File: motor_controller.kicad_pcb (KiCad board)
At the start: 2 copper layers, 251.5 x 106.7 mm, 134 parts, among them J1 STM32F4_Discovery_Header, J10 Conn_01x02_Male, J11 Conn_01x02_Male, J12 Conn_01x03_Male, J13 Conn_01x06_Male, J14 Conn_01x02_Male, J15 Conn_01x02_Male, J16 pololu-D24V10F5, J17 Conn_01x02_Male, J2 Conn_01x02_Male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

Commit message: Add memes. Also fix silkscreen
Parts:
- added G***: LOGO, roboarm_kicadlib:spanish, F.Cu at (73.7, 116.2)
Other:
- board text added: "Jos tää kaataa skumppaa stimussa niin sit mä oon vittu nähnyt kaiken. Kahdesti. -Eipou"
- board text added: "Roboarm Motor Controller Revision A Eipou 2018"

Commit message: Add controller din mount part and 3D model
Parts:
- removed G***: LOGO, roboarm_kicadlib:spanish
- removed MH3, MH4: MountingHole, MountingHole:MountingHole_3.2mm_M3_DIN965
- MH1, MH2: value MountingHole -> DinMount; footprint MountingHole:MountingHole_3.2mm_M3_DIN965 -> roboarm_kicadlib:controller_din_mount
- moved MH1 48.2 mm to (20.3, 106.7)
- moved MH2 48.2 mm to (261.6, 106.7)

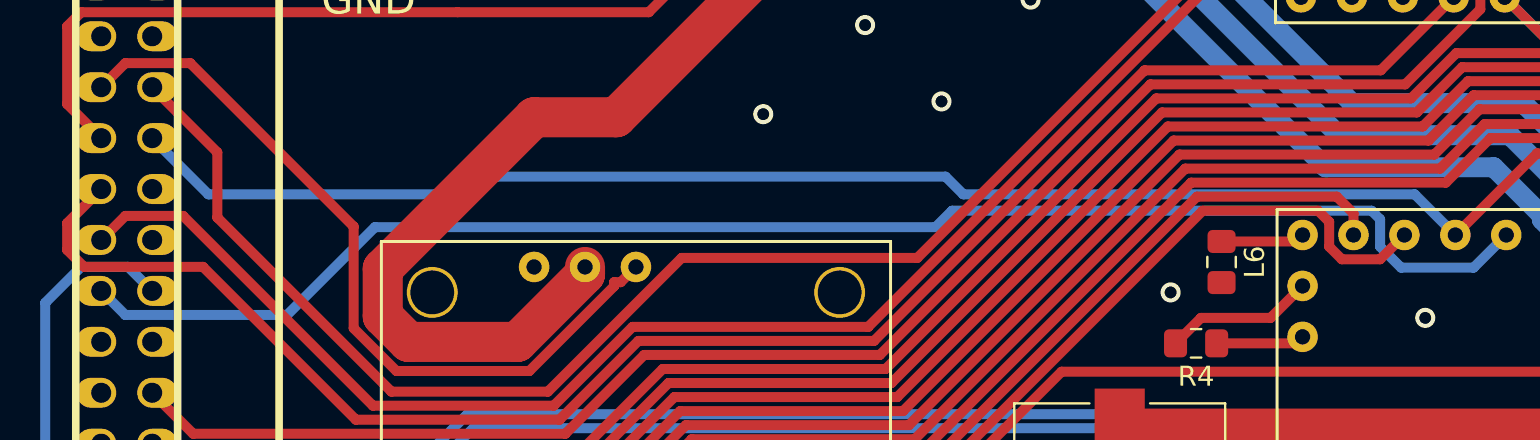
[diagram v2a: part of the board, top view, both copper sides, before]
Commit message: Add pulldown to ~motor_sleep_all
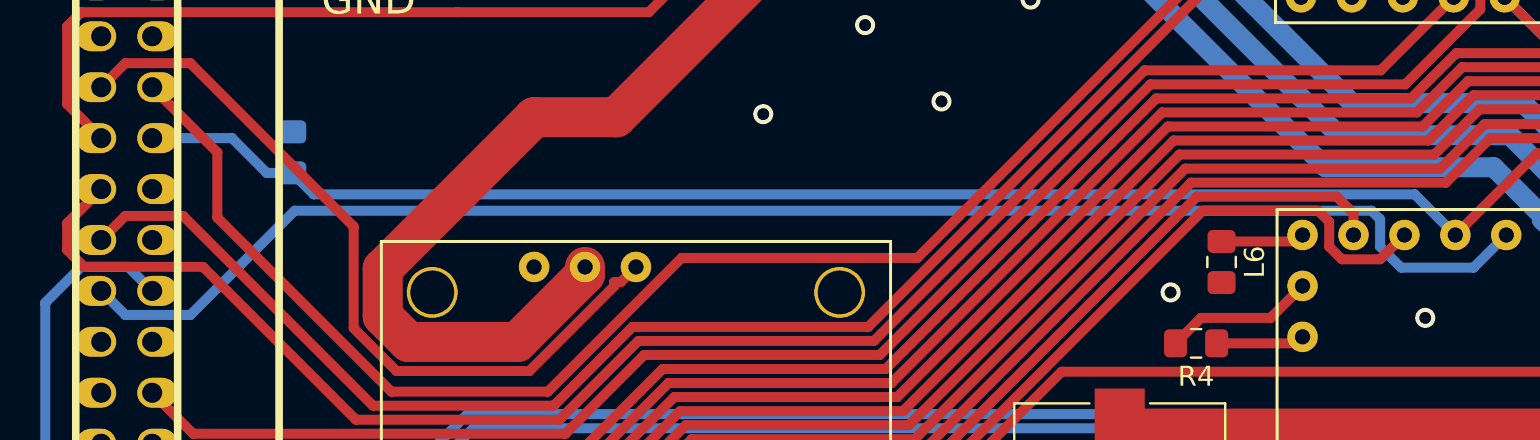
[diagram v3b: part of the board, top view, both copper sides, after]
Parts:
- added R13: 330R, Resistor_SMD:R_0805_2012Metric_Pad1.15x1.40mm_HandSolder, B.Cu at (107.3, 108.0)
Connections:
- C18 pad 1: motor_pot_2 -> motor_pot_1
- C19 pad 1: motor_pot_4 -> motor_pot_3
- C20 pad 1: motor_pot_6 -> motor_pot_5
- C21 pad 1: motor_pot_1 -> motor_pot_2
- C22 pad 1: motor_pot_3 -> motor_pot_4
- C23 pad 1: motor_pot_5 -> motor_pot_6
- J1 pad 11: motor_pot_1 -> motor_pot_2
- J1 pad 13: motor_pot_4 -> motor_pot_3
- J1 pad 15: motor_pot_3 -> motor_pot_4
- J1 pad 19: motor_pot_6 -> motor_pot_5
- J1 pad 21: motor_pot_5 -> motor_pot_6
- J1 pad 7: motor_pot_2 -> motor_pot_1
- L11 pad 1: motor_pot_1 -> motor_pot_2
- L12 pad 2: motor_pot_2 -> motor_pot_1
- L13 pad 1: motor_pot_3 -> motor_pot_4
- L14 pad 2: motor_pot_4 -> motor_pot_3
- L15 pad 1: motor_pot_5 -> motor_pot_6
- L16 pad 2: motor_pot_6 -> motor_pot_5
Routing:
- net motor_pot_6: track 32.3 -> 37.5 mm
- net motor_pot_5: track 37.5 -> 32.3 mm
- net motor_pot_4: track 24.9 -> 29.6 mm
- net motor_pot_3: track 29.6 -> 24.9 mm
- net motor_pot_2: track 17.4 -> 19.8 mm
- net motor_pot_1: track 19.8 -> 17.4 mm
- net motor_sleep_all: track 227.7 -> 226.9 mm

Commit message: Rename ~motor_sleep to motor_enable
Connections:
- net motor_sleep_all renamed motor_enable_all

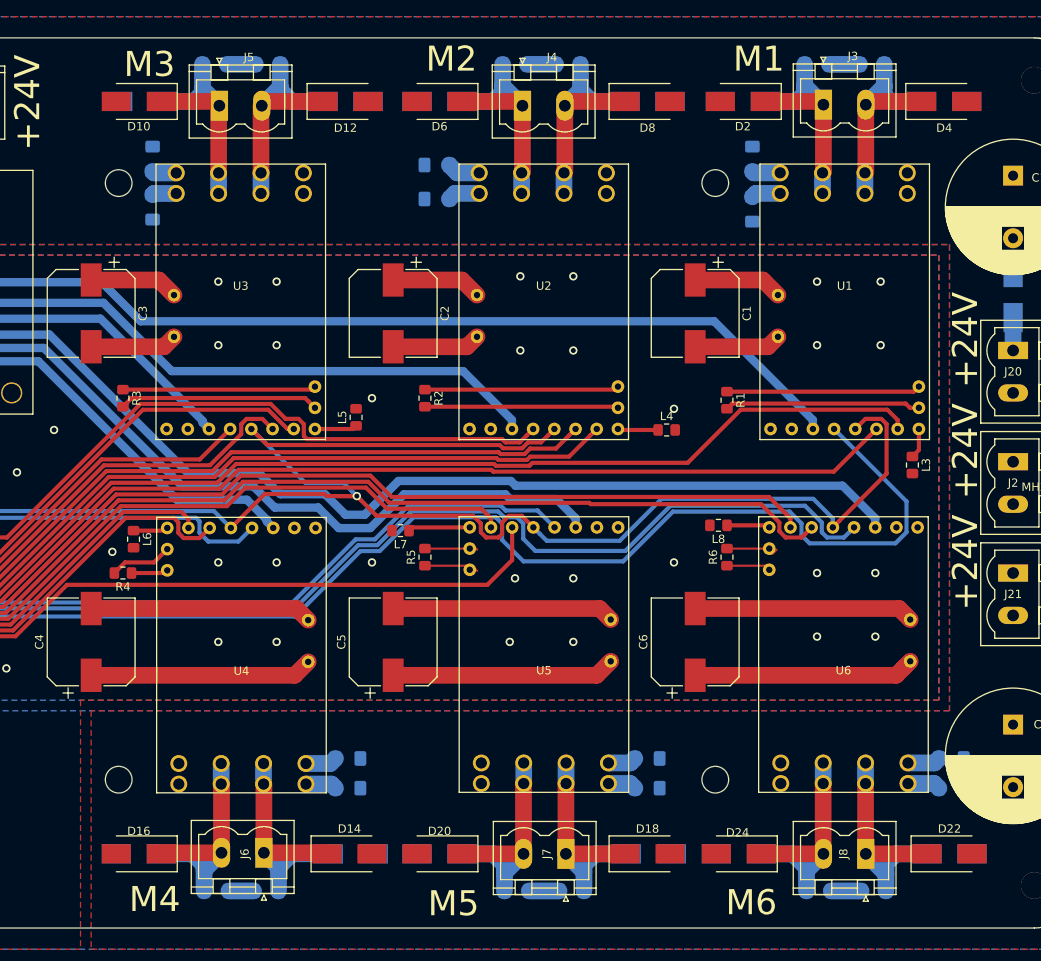
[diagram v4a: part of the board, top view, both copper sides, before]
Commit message: Change RC-Snubber footprints
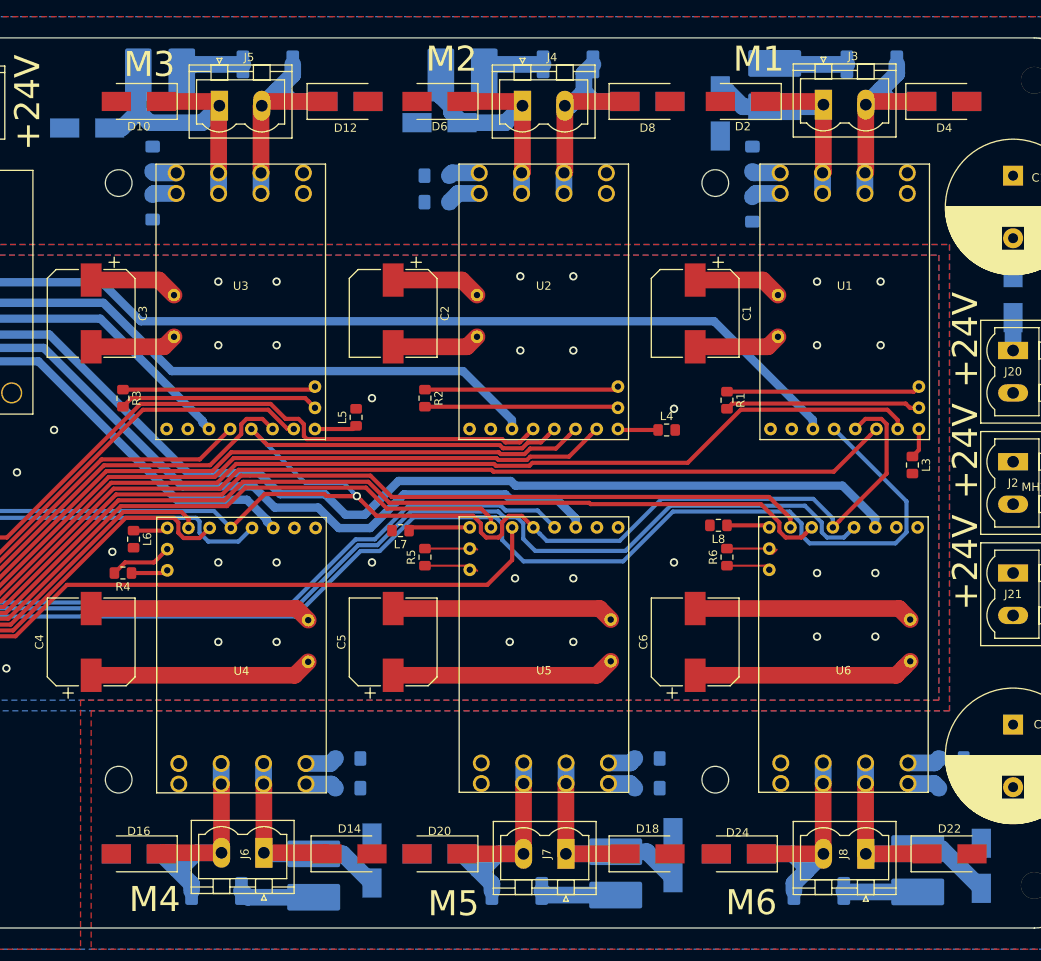
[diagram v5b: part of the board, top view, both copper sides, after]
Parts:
- C12, C13, C14, C15, C16, C17: value C -> C_Snubber; footprint Capacitor_SMD:C_1206_3216Metric_Pad1.42x1.75mm_HandSolder -> roboarm_kicadlib:C_2824_7260Metric_Pad3.20x6.35mm_HandSolder
- R10, R11, R12, R7, R8, R9: value R -> R_Snubber; footprint Resistor_SMD:R_1206_3216Metric_Pad1.42x1.75mm_HandSolder -> Resistor_SMD:R_2512_6332Metric_Pad1.52x3.35mm_HandSolder
- moved D11 7.10 mm to (148.1, 64.1)
- moved C14 6.69 mm to (156.8, 57.8)
- moved C13 6.42 mm to (193.1, 57.8)
- moved C15 6.01 mm to (175.3, 153.7), turned to 90 degrees
- moved C17 5.85 mm to (247.7, 153.1), turned to 90 degrees
- moved C16 5.70 mm to (211.5, 153.5), turned to 90 degrees
- moved C12 5.65 mm to (230.5, 59.0), turned to 270 degrees
- moved D23 4.07 mm to (255.3, 152.6), turned to 270 degrees
- moved D3 3.06 mm to (224.0, 62.4), turned to 90 degrees
- moved D19 2.89 mm to (218.3, 151.3), turned to 270 degrees
- moved D15 2.66 mm to (182.2, 151.9), turned to 270 degrees
- moved D7 2.54 mm to (190.3, 63.5)
- moved C26 1.27 mm to (190.0, 69.8)
- moved C27 0.38 mm to (190.0, 73.0)
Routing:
- net Net-(C14-Pad2): track 29.2 -> 37.4 mm
- net Net-(C15-Pad1): track 2.96 -> 8.97 mm
- net Net-(C16-Pad1): track 3.57 -> 9.07 mm
- net Net-(C17-Pad1): track 3.58 -> 8.91 mm
- net Net-(C12-Pad1): track 3.59 -> 8.71 mm
- net Net-(C14-Pad1): track 3.38 -> 7.86 mm
- net Net-(C17-Pad2): track 30.3 -> 34.3 mm
- net Net-(C13-Pad1): track 3.38 -> 7.32 mm
- net Net-(C13-Pad2): track 30.0 -> 33.5 mm
- net Net-(C15-Pad2): track 30.3 -> 32.8 mm
- net Net-(C16-Pad2): track 29.8 -> 32.2 mm
- net Net-(C12-Pad2): track 29.6 -> 31.0 mm
- net Net-(D12-Pad1): track 30.0 -> 30.7 mm
- net Net-(D24-Pad1): track 30.1 -> 30.7 mm

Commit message: Clean schematics, add schematic notes
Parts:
- C12, C13, C14, C15, C16, C17: value C_Snubber -> 100n
- R10, R11, R12, R7, R8, R9: value R_Snubber -> 100R

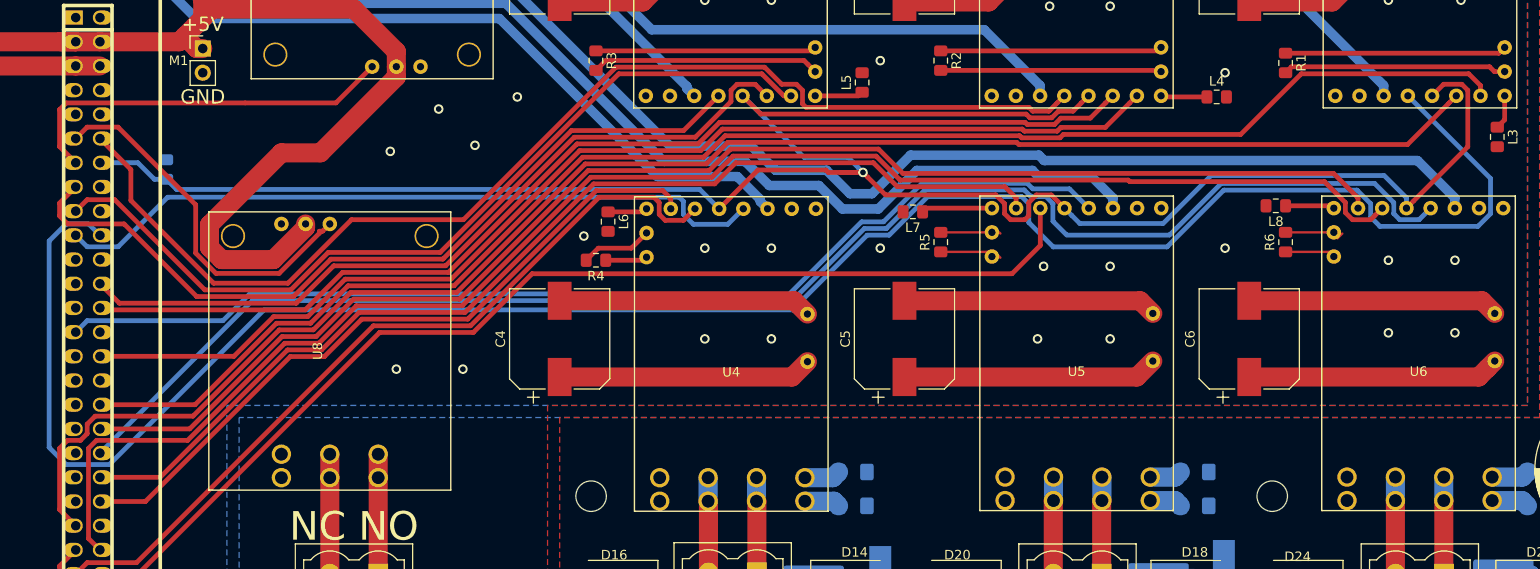
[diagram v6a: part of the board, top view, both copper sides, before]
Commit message: Rearrange motor dir pins
Two of the motor direction pins conflict with JTAG.
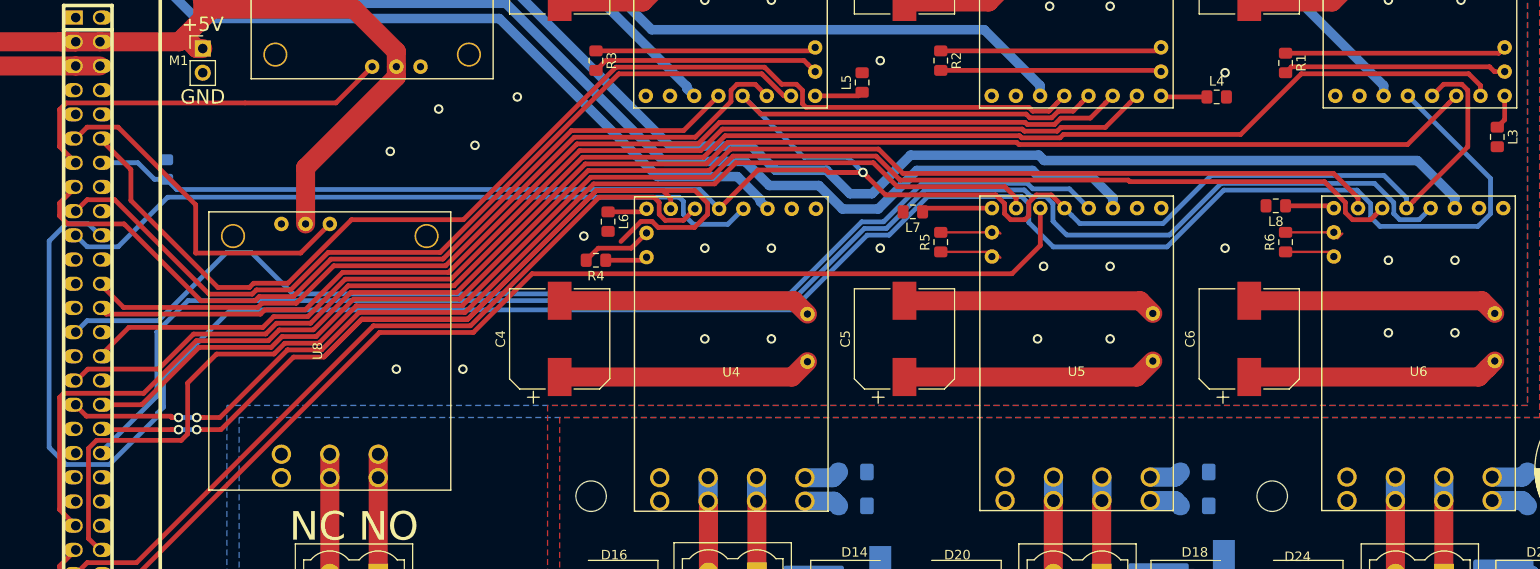
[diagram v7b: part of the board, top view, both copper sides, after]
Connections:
- J1 pad 60: motor_dir_4 -> Net-(J1-Pad60)
- J1 pad 62: motor_dir_5 -> Net-(J1-Pad62)
- J1 pad 66: motor_dir_6 -> motor_dir_4
- J1 pad 67: Net-(J1-Pad67) -> motor_dir_5
- J1 pad 68: motor_dir_1 -> motor_dir_6
- J1 pad 69: Net-(J1-Pad69) -> motor_dir_1
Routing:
- net motor_dir_4: track 74.9 -> 131.7 mm, vias 0 -> 2
- net +5V: track 182.4 -> 161.0 mm
- net motor_fault_6: track 159.2 -> 163.1 mm
- net motor_fault_5: track 113.9 -> 117.5 mm
- net motor_pwm_6: track 163.6 -> 166.7 mm
- net motor_pwm_1: track 171.5 -> 174.1 mm
- net motor_fault_1: track 216.7 -> 218.8 mm
- net relay_gripper: track 38.8 -> 36.9 mm
- net motor_dir_1: track 161.1 -> 162.6 mm
- net motor_dir_6: track 147.4 -> 146.4 mm
- net motor_dir_5: track 112.5 -> 113.0 mm, vias 0 -> 2
